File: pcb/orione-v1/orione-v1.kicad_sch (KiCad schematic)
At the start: 15 parts, among them J1 Conn_02x10_Odd_Even, J2 Conn_02x10_Odd_Even, J3 Conn_02x03_Odd_Even

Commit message: pcv v1.1
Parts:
- removed J3: Conn_02x03_Odd_Even, Connector_PinHeader_2.54mm:PinHeader_2x03_P2.54mm_Horizontal, symbol Connector_Generic:Conn_02x03_Odd_Even
- added J3: Conn_01x06_Pin, Connector_PinHeader_2.54mm:PinHeader_1x06_P2.54mm_Horizontal, symbol Connector:Conn_01x06_Pin
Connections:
- net Row 0: now also J2.8 (Pin_8); no longer J1.13 (Pin_13)
- net Row 1: now also J2.12 (Pin_12); no longer J1.11 (Pin_11)
- net Row 2: now also J2.14 (Pin_14); no longer J1.9 (Pin_9)
- net Row 3: now also J2.16 (Pin_16); no longer J1.7 (Pin_7)
- net Row 4: now also J2.18 (Pin_18); no longer J1.5 (Pin_5)
- net Row 5: now also J2.20 (Pin_20); no longer J1.3 (Pin_3)
- net at H1.1, H2.1, H3.1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: now also D89.1 (K), D90.1 (K), J1.4 (Pin_4); no longer J1.19 (Pin_19)
- net at J1.1 (Pin_1): now also J3.3 (Pin_3)
- net at R1.2: now also J2.6 (Pin_6); no longer J2.4 (Pin_4)
- net at J2.2 (Pin_2): now also J3.1 (Pin_1); no longer R2.2
- new net: J1.11 (Pin_11), J3.2 (Pin_2)
- new net: J1.5 (Pin_5), J3.5 (Pin_5)
- new net: J1.7 (Pin_7), J3.4 (Pin_4)
- new net: J1.9 (Pin_9), J3.6 (Pin_6)
- new net: J2.4 (Pin_4), R2.2
- no-connect marks 13 -> 8

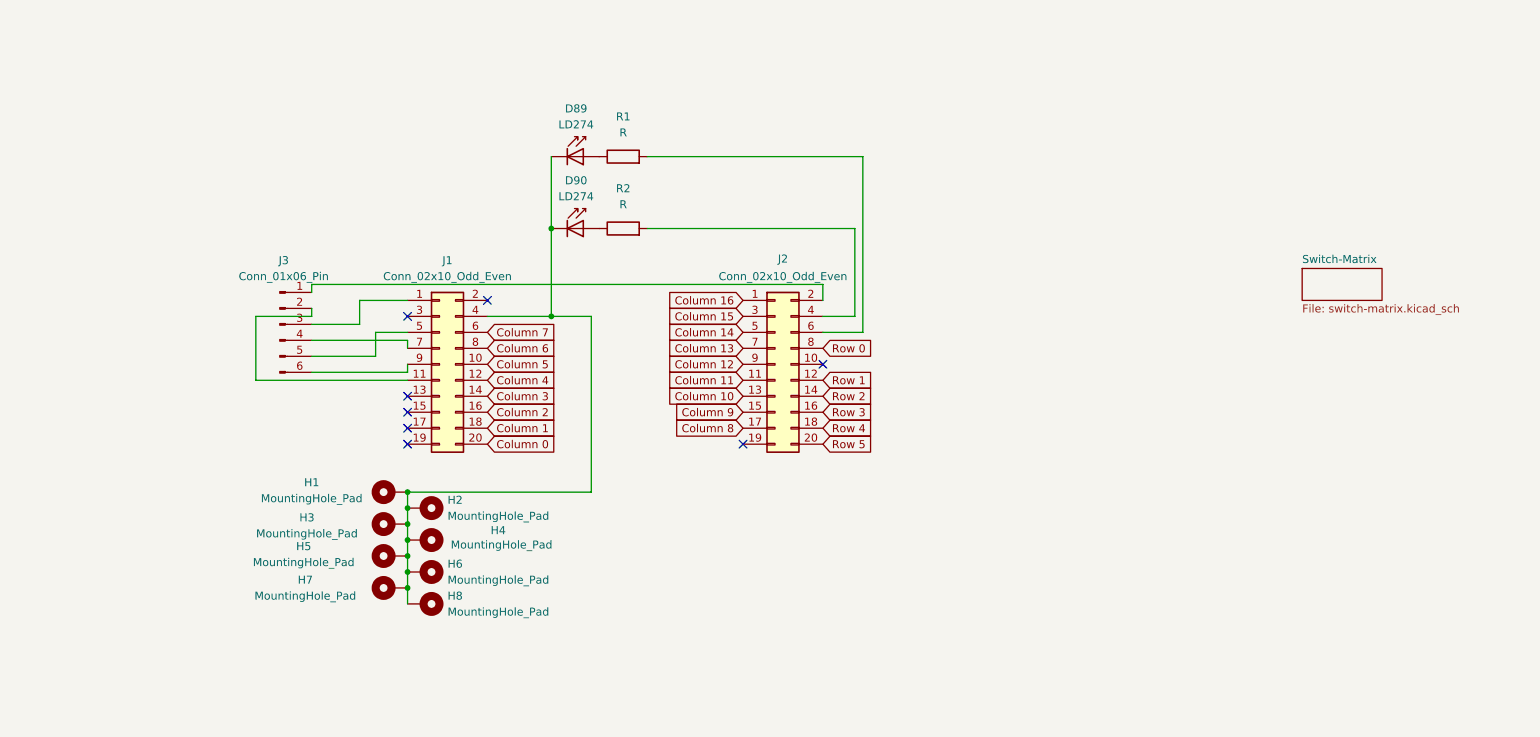
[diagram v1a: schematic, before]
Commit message: fixed GND
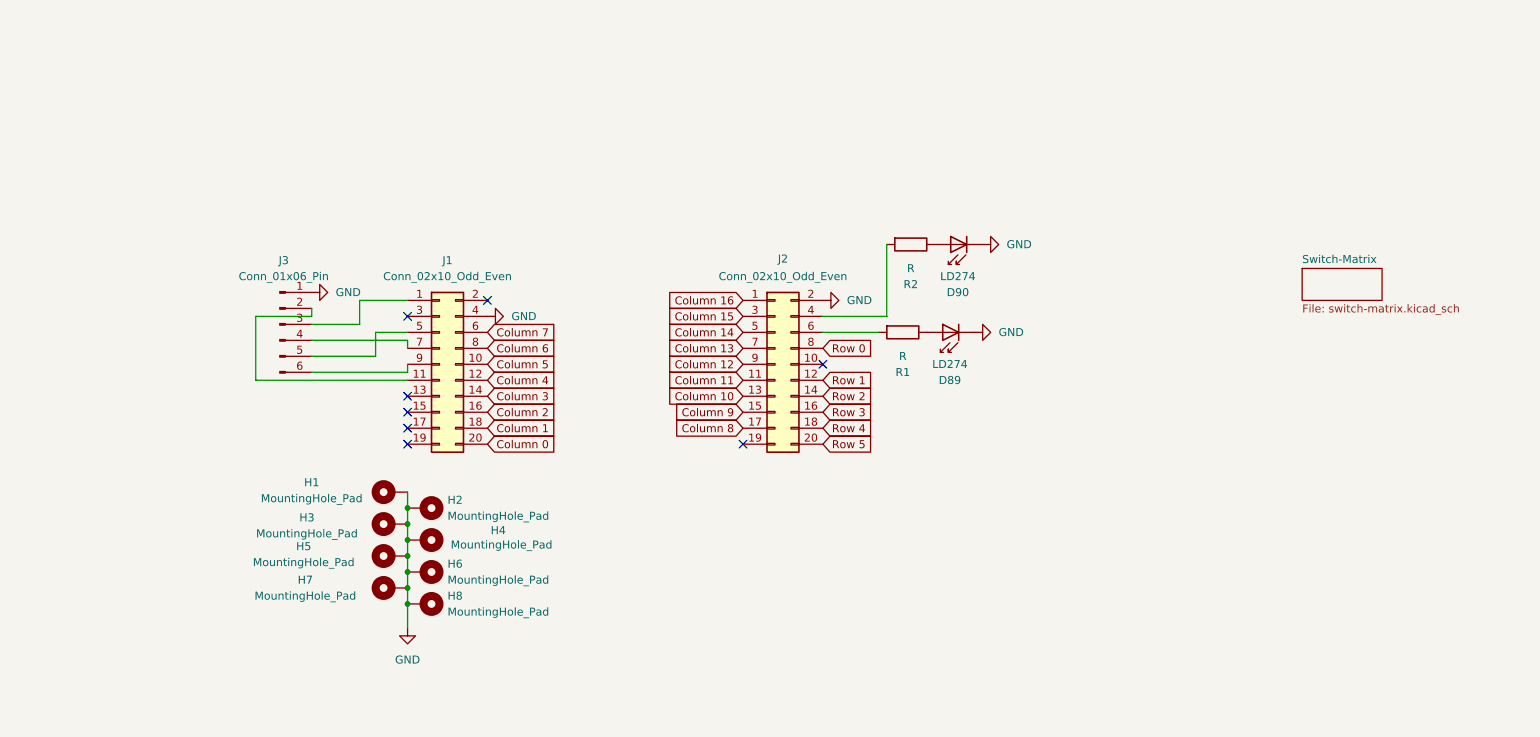
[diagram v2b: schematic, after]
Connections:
- net GND: now reaches D89.1 (K), D90.1 (K), H1.1, H2.1, H3.1, H4.1, H5.1, H6.1, H7.1, H8.1, J1.4 (Pin_4)
- net GND: now also J2.2 (Pin_2), J3.1 (Pin_1)
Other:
- moved on the sheet: D90, R2

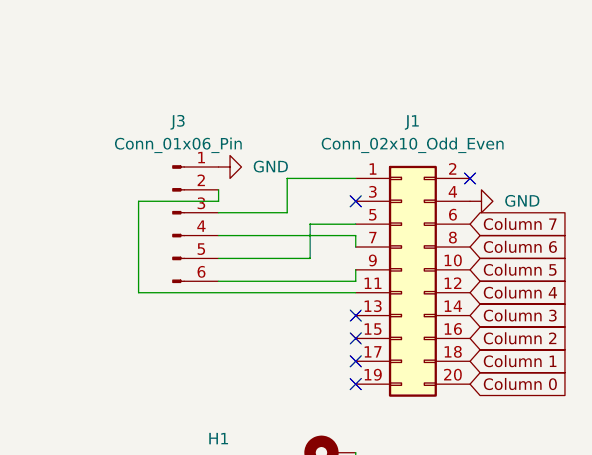
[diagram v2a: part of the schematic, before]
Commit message: added voltage divider
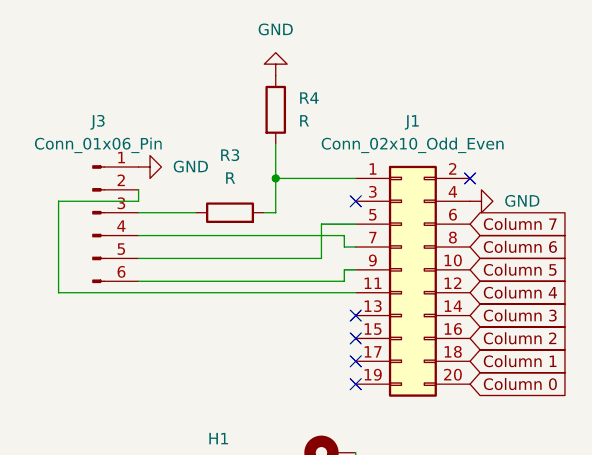
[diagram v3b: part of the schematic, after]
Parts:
- added R3, R4: R, Resistor_THT:R_Axial_DIN0207_L6.3mm_D2.5mm_P10.16mm_Horizontal, symbol Device:R
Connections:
- net GND: now also R4.1
- net at J3.3 (Pin_3): now also R3.1; no longer J1.1 (Pin_1)
- new net: J1.1 (Pin_1), R3.2, R4.2
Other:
- moved on the sheet: J3

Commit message: changed pin layout of uart
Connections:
- net at J1.11 (Pin_11): no longer J3.2 (Pin_2)
- net at J1.3 (Pin_3): now also J3.2 (Pin_2)
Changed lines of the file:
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@@
-	)
-	(no_connect
-		(at 90.17 87.63)
 	)
 	(no_connect
@@
 	(no_connect
 		(at 102.87 85.09)
+	)
+	(no_connect
+		(at 90.17 97.79)
 	)
 	(no_connect
@@
 		(pts
 			(xy 166.37 87.63) (xy 166.37 76.2)
-		)
-		(stroke
-			(width 0)
-			(type default)
-		)
-	)
-	(wire
-		(pts
-			(xy 57.15 97.79) (xy 90.17 97.79)
 		)
 		(stroke
@@
 	(wire
 		(pts
-			(xy 66.04 86.36) (xy 66.04 87.63)
+			(xy 90.17 120.65) (xy 90.17 123.19)
 		)
 		(stroke
@@
 	(wire
 		(pts
-			(xy 90.17 120.65) (xy 90.17 123.19)
+			(xy 90.17 86.36) (xy 90.17 87.63)
 		)
 		(stroke
@@
 	(wire
 		(pts
-			(xy 66.04 87.63) (xy 57.15 87.63)
-		)
-		(stroke
-			(width 0)
-			(type default)
-		)
-	)
-	(wire
-		(pts
 			(xy 88.9 91.44) (xy 88.9 92.71)
 		)
@@
 		(pts
 			(xy 88.9 95.25) (xy 90.17 95.25)
-		)
-		(stroke
-			(width 0)
-			(type default)
-		)
-	)
-	(wire
-		(pts
-			(xy 57.15 87.63) (xy 57.15 97.79)
 		)
 		(stroke
@@
 		)
 		(stroke
+			(width 0)
+			(type default)
+		)
+	)
+	(wire
+		(pts
+			(xy 66.04 86.36) (xy 90.17 86.36)
+		)
+		(stroke

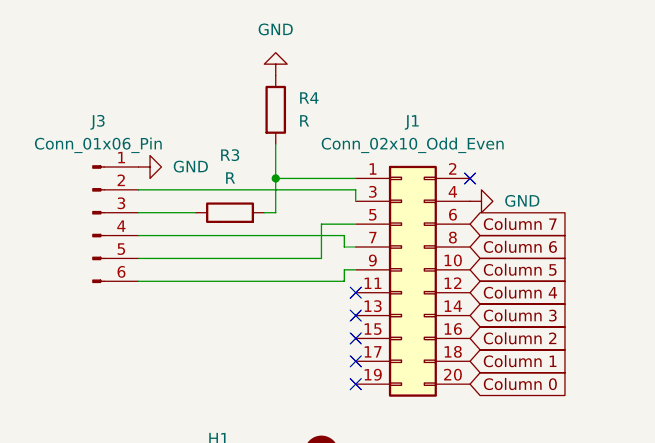
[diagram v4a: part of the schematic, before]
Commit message: modified pcb based on new parts
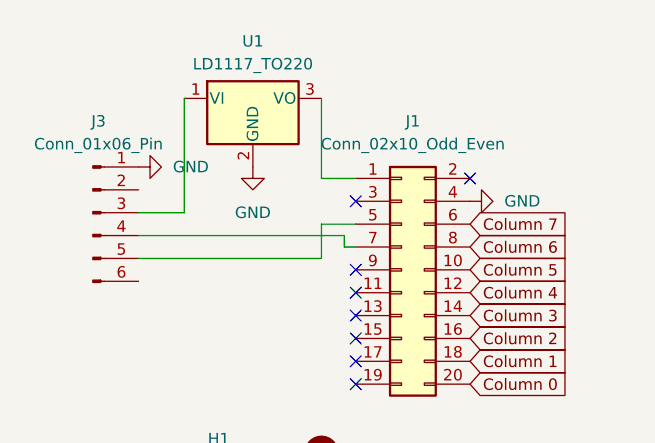
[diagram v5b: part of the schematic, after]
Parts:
- removed R3, R4: R, Resistor_THT:R_Axial_DIN0207_L6.3mm_D2.5mm_P10.16mm_Horizontal, symbol Device:R
- added U1: LD1117_TO220, Package_TO_SOT_THT:TO-220-3_Vertical, symbol Regulator_Linear:LF15_TO220
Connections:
- net GND: now also U1.2 (GND)
- net at J3.3 (Pin_3): now also U1.1 (VI)
- net at J1.1 (Pin_1): now also U1.3 (VO)
- net at J1.3 (Pin_3): no longer J3.2 (Pin_2)
- net at J1.9 (Pin_9): no longer J3.6 (Pin_6)
- no-connect marks 8 -> 10

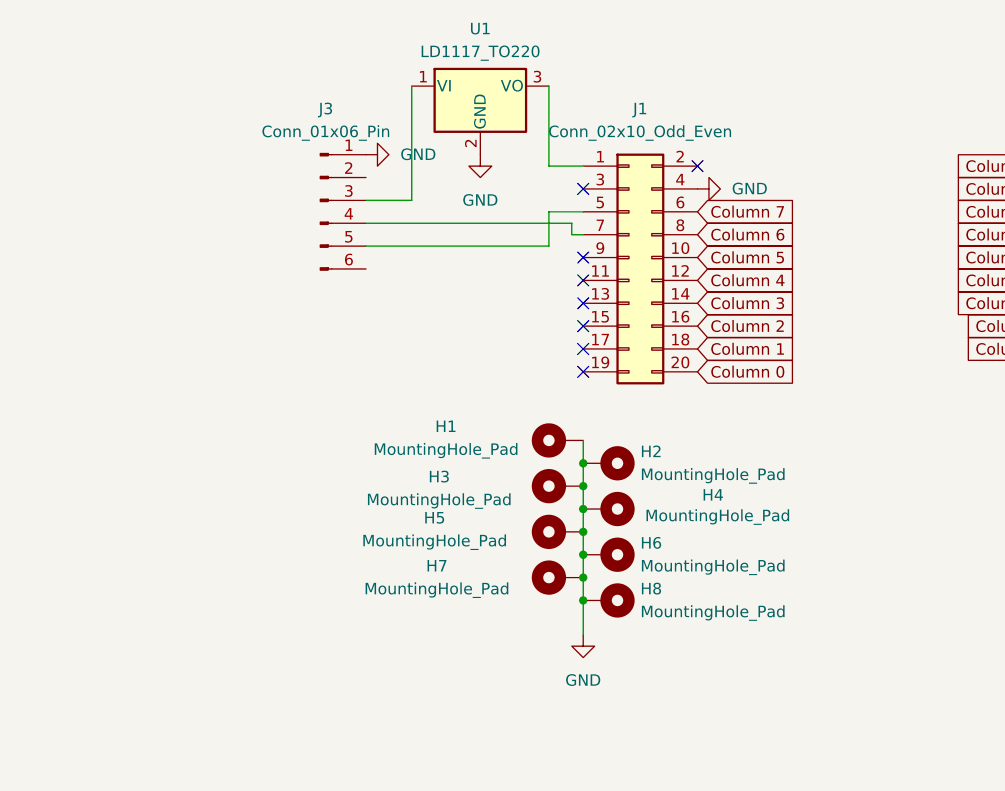
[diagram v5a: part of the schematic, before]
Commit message: added to pcb rotary encoder and oled dysplay
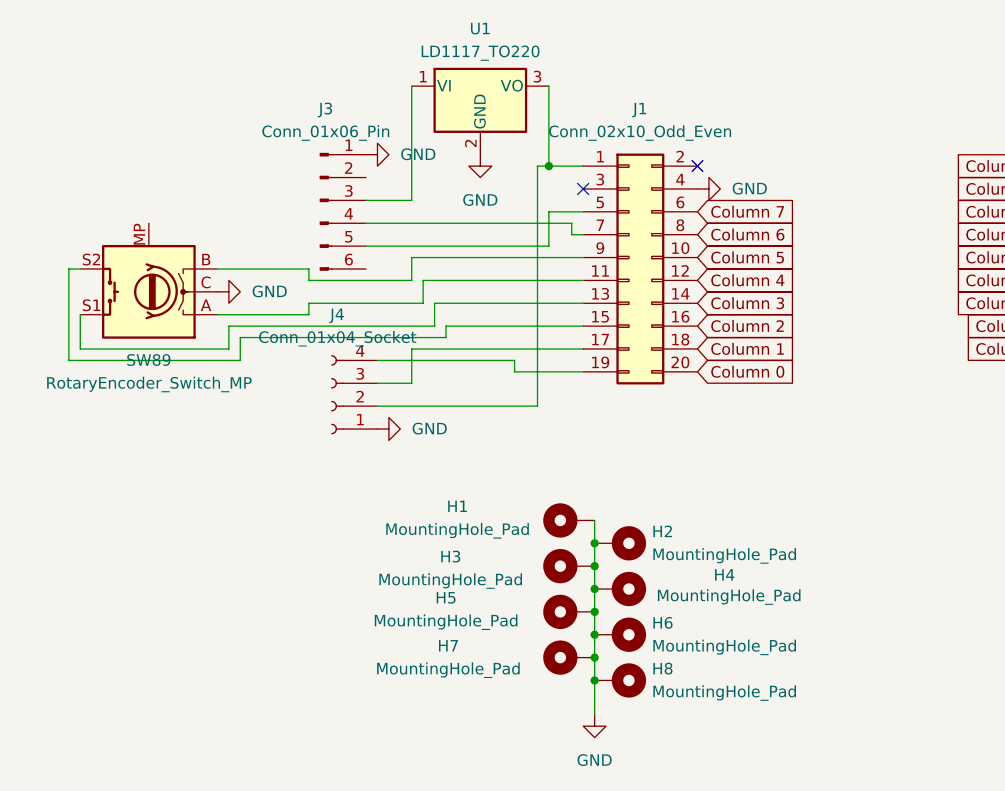
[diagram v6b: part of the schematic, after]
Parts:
- added J4: Conn_01x04_Socket, Connector_PinSocket_2.54mm:PinSocket_1x04_P2.54mm_Vertical, symbol Connector:Conn_01x04_Socket
- added SW89: RotaryEncoder_Switch_MP, Rotary_Encoder:RotaryEncoder_Bourns_Vertical_PEC12R-3x17F-Sxxxx, symbol Device:RotaryEncoder_Switch_MP
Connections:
- net GND: now also J4.1 (Pin_1), SW89.C
- net at J1.1 (Pin_1), U1.3 (VO): now also J4.2 (Pin_2)
- net at J1.11 (Pin_11): now also SW89.A
- net at J1.13 (Pin_13): now also SW89.S1
- net at J1.15 (Pin_15): now also SW89.S2
- net at J1.17 (Pin_17): now also J4.3 (Pin_3)
- net at J1.19 (Pin_19): now also J4.4 (Pin_4)
- net at J1.9 (Pin_9): now also SW89.B
- no-connect marks 10 -> 4
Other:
- moved on the sheet: H1, H2, H3, H4, H5, H6, H7, H8

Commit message: prova
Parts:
- removed H1, H2, H3, H4, H5, H6, H7, H8: MountingHole_Pad, MountingHole:MountingHole_3.2mm_M3_Pad_Via, symbol Mechanical:MountingHole_Pad
- removed J4: Conn_01x04_Socket, Connector_PinSocket_2.54mm:PinSocket_1x04_P2.54mm_Vertical, symbol Connector:Conn_01x04_Socket
- removed SW89: RotaryEncoder_Switch_MP, Rotary_Encoder:RotaryEncoder_Bourns_Vertical_PEC12R-3x17F-Sxxxx, symbol Device:RotaryEncoder_Switch_MP
- removed U1: LD1117_TO220, Package_TO_SOT_THT:TO-220-3_Vertical, symbol Regulator_Linear:LF15_TO220
- added C1, C2: C_Polarized, Capacitor_THT:CP_Radial_Tantal_D4.5mm_P5.00mm, symbol Device:C_Polarized
- added C3, C4, C5, C6: C, Capacitor_THT:C_Radial_D10.0mm_H12.5mm_P5.00mm, symbol Device:C
- added SW90: RotaryEncoder, Rotary_Encoder:RotaryEncoder_Alps_EC12E_Vertical_H20mm, symbol Device:RotaryEncoder
- added U2: TLV1117-50, Package_TO_SOT_THT:TO-220-3_Vertical, symbol Regulator_Linear:TLV1117-50
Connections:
- net GND: now also C1.2, C2.2, C3.2, C4.2, C5.2, C6.2, SW90.C, U2.1 (GND)
- net at J1.11 (Pin_11): now also SW90.A
- net at J1.9 (Pin_9): now also SW90.B
- net at J1.1 (Pin_1): now also C2.1, C5.1, C6.1, U2.2 (VO)
- net at J3.3 (Pin_3): now also C1.1, C3.1, C4.1, U2.3 (VI)
- no-connect marks 4 -> 10
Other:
- moved on the sheet: J3

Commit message: should work
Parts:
- C3, C4, C5, C6: footprint Capacitor_THT:C_Radial_D10.0mm_H12.5mm_P5.00mm -> Capacitor_THT:C_Radial_D4.0mm_H7.0mm_P1.50mm
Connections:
- net at C2.1, C5.1, C6.1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: now also R1.2
- net at J2.6 (Pin_6): no longer R1.2
- no-connect marks 10 -> 11
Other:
- moved on the sheet: D89, R1
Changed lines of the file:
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@@
 (kicad_sch
-	(version 20231120)
+	(version 20250114)
 	(generator "eeschema")
-	(generator_version "8.0")
+	(generator_version "9.0")
 	(paper "A4")
 	(junction
@@
 	)
 	(junction
+		(at 99.06 46.99)
+		(diameter 0)
+		(color 0 0 0 0)
+	)
+	(junction
 		(at 95.25 46.99)
 		(diameter 0)
@@
 	)
 	(no_connect
+		(at 156.21 90.17)
+	)
+	(no_connect
 		(at 102.87 85.09)
 	)
@@
 	(wire
 		(pts
+			(xy 95.25 46.99) (xy 99.06 46.99)
+		)
+		(stroke
+			(width 0)
+			(type default)
+		)
+	)
+	(wire
+		(pts
 			(xy 76.2 46.99) (xy 76.2 48.26)
 		)
@@
 	(wire
 		(pts
-			(xy 95.25 46.99) (xy 99.06 46.99)
-		)
-		(stroke
-			(width 0)
-			(type default)
-		)
-	)
-	(wire
-		(pts
 			(xy 90.17 85.09) (xy 83.82 85.09)
 		)
@@
 	(wire
 		(pts
+			(xy 99.06 46.99) (xy 110.49 46.99)
+		)
+		(stroke
+			(width 0)
+			(type default)
+		)
+	)
+	(wire
+		(pts
 			(xy 38.1 46.99) (xy 38.1 48.26)
 		)
@@
 		(pts
 			(xy 66.04 54.61) (xy 66.04 58.42)
-		)
-		(stroke
-			(width 0)
-			(type default)
-		)
-	)
-	(wire
-		(pts
-			(xy 156.21 90.17) (xy 165.1 90.17)
 		)
 		(stroke
@@
 			)
 		)
-		(property "Footprint" "Capacitor_THT:C_Radial_D10.0mm_H12.5mm_P5.00mm"
+		(property "Footprint" "Capacitor_THT:C_Radial_D4.0mm_H7.0mm_P1.50mm"
 			(at 46.6852 55.88 0)
 			(effects
@@
 			)
 		)
-		(property "Footprint" "Capacitor_THT:C_Radial_D10.0mm_H12.5mm_P5.00mm"
+		(property "Footprint" "Capacitor_THT:C_Radial_D4.0mm_H7.0mm_P1.50mm"
 			(at 86.0552 55.88 0)
 			(effects
@@
 	(symbol
 		(lib_id "LED:LD274")
-		(at 175.26 90.17 180)
+		(at 120.65 46.99 180)
 		(unit 1)
 		(exclude_from_sim no)
@@
 		(fields_autoplaced yes)
 		(property "Reference" "D89"
-			(at 176.403 97.79 0)
+			(at 121.793 54.61 0)
 			(effects
 				(font
@@
 		)
 		(property "Value" "LD274"
-			(at 176.403 95.25 0)
+			(at 121.793 52.07 0)
 			(effects
 				(font
@@
 		)
 		(property "Footprint" "LED_THT:LED_D5.0mm_IRGrey"
-			(at 175.26 94.615 0)
+			(at 120.65 51.435 0)
 			(effects
 				(font
@@
 		)
 		(property "Datasheet" "http://pdf.datasheetcatalog.com/datasheet/siemens/LD274.pdf"
-			(at 176.53 90.17 0)
+			(at 121.92 46.99 0)
 			(effects
 				(font
@@
 		)
 		(property "Description" "950nm IR-LED, 5mm"
-			(at 175.26 90.17 0)
+			(at 120.65 46.99 0)
 			(effects
 				(font
@@
 			)
 		)
-		(property "Footprint" "Capacitor_THT:C_Radial_D10.0mm_H12.5mm_P5.00mm"
+		(property "Footprint" "Capacitor_THT:C_Radial_D4.0mm_H7.0mm_P1.50mm"
 			(at 55.5752 55.88 0)
 			(effects
@@
 			)
 		)
-		(property "Footprint" "Capacitor_THT:C_Radial_D10.0mm_H12.5mm_P5.00mm"
+		(property "Footprint" "Capacitor_THT:C_Radial_D4.0mm_H7.0mm_P1.50mm"
 			(at 77.1652 55.88 0)
 			(effects
@@
 	(symbol
 		(lib_id "power:GND")
-		(at 180.34 90.17 90)
+		(at 125.73 46.99 90)
 		(unit 1)
 		(exclude_from_sim no)
@@
 		(fields_autoplaced yes)
 		(property "Reference" "#PWR05"
-			(at 186.69 90.17 0)
+			(at 132.08 46.99 0)
 			(effects
 				(font
@@
 		)
 		(property "Value" "GND"
-			(at 184.15 90.1701 90)
+			(at 129.54 46.9901 90)
 			(effects
 				(font
@@
 		)
 		(property "Footprint" ""
-			(at 180.34 90.17 0)
+			(at 125.73 46.99 0)
 			(effects
 				(font
@@
 		)
 		(property "Datasheet" ""
-			(at 180.34 90.17 0)
+			(at 125.73 46.99 0)
 			(effects
 				(font
@@
 		)
 		(property "Description" "Power symbol creates a global label with name \"GND\" , ground"
-			(at 180.34 90.17 0)
+			(at 125.73 46.99 0)
 			(effects
 				(font
@@
 	(symbol
 		(lib_id "Device:R")
-		(at 168.91 90.17 270)
+		(at 114.3 46.99 270)
 		(unit 1)
 		(exclude_from_sim no)
@@
 		(fields_autoplaced yes)
 		(property "Reference" "R1"
-			(at 168.91 96.52 90)
+			(at 114.3 53.34 90)
 			(effects
 				(font
@@
 		)
 		(property "Value" "R"
-			(at 168.91 93.98 90)
+			(at 114.3 50.8 90)
 			(effects
 				(font
@@
 		)
 		(property "Footprint" "Resistor_THT:R_Axial_DIN0207_L6.3mm_D2.5mm_P10.16mm_Horizontal"
-			(at 168.91 88.392 90)
+			(at 114.3 45.212 90)
 			(effects
 				(font
@@
 		)
 		(property "Datasheet" "~"
-			(at 168.91 90.17 0)
+			(at 114.3 46.99 0)
 			(effects
 				(font
@@
 		)
 		(property "Description" "Resistor"
-			(at 168.91 90.17 0)
+			(at 114.3 46.99 0)
 			(effects
 				(font
@@
 		(at 84.455 129.54)
 		(size 12.7 9.525)
+		(exclude_from_sim no)
+		(in_bom yes)
+		(on_board yes)
+		(dnp no)
 		(fields_autoplaced yes)
 		(stroke
@@
 		)
 	)
+	(embedded_fonts no)
 )
